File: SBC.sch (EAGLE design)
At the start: 42 parts, among them IC1 MAX3232CPE, IC2 74LS04N, IC3 74LS00N, IC5 NE555P, J1 POWER_JACKPTH, J2 COMPUTER-PERIPHERAL-POWERRA, J3 22-27-2021-02

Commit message: Added gerber files
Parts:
- C7: value (none) -> 10uF
- RAM: value (none) -> 62256
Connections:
- removed net N$32: IC1G$1.T1IN
- removed net N$33: ACIAG$1.RXC, IC1G$1.T1OUT
- removed net RINGINDICATOR: X1.9
- removed net TRANSMITDATA: IC1G$1.R2OUT, X1.3
- new net DATASETREADY: ACIAG$1./DSR, X1.6
- new net N$1: LED1.C, R5.1
- new net N$3: IC1G$1.T1OUT, X1.3
- new net N$5: ACIAG$1.R/W, CPUG$1.R/W
- new net N$7: ACIAG$1.TXD, IC1G$1.T1IN
- new net N$8: ACIAG$1.RXD, IC1G$1.R1OUT
- net DATACARRIERDETECT: now also ACIAG$1./DCD; no longer X1.6
- net DTEREADY: no longer IC1G$1.R2IN
- net GND: now also RAM.VSS, X1.9; no longer ACIAG$1./DCD, ACIAG$1./DSR
- net IRQ: now also ACIAG$1./IRQ, VIA0G$1./IRQ
- net N$17: now also VIA0G$1./CS2
- net RECEIVEDATA: now also IC1G$1.R1IN
- net VCC: now also RAM.VCC; no longer LED1.C, R5.1
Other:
- moved on the sheet: ACIA, C1, C2, C3, C4, C5, C6, C7, C8, C9, CPU, D1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

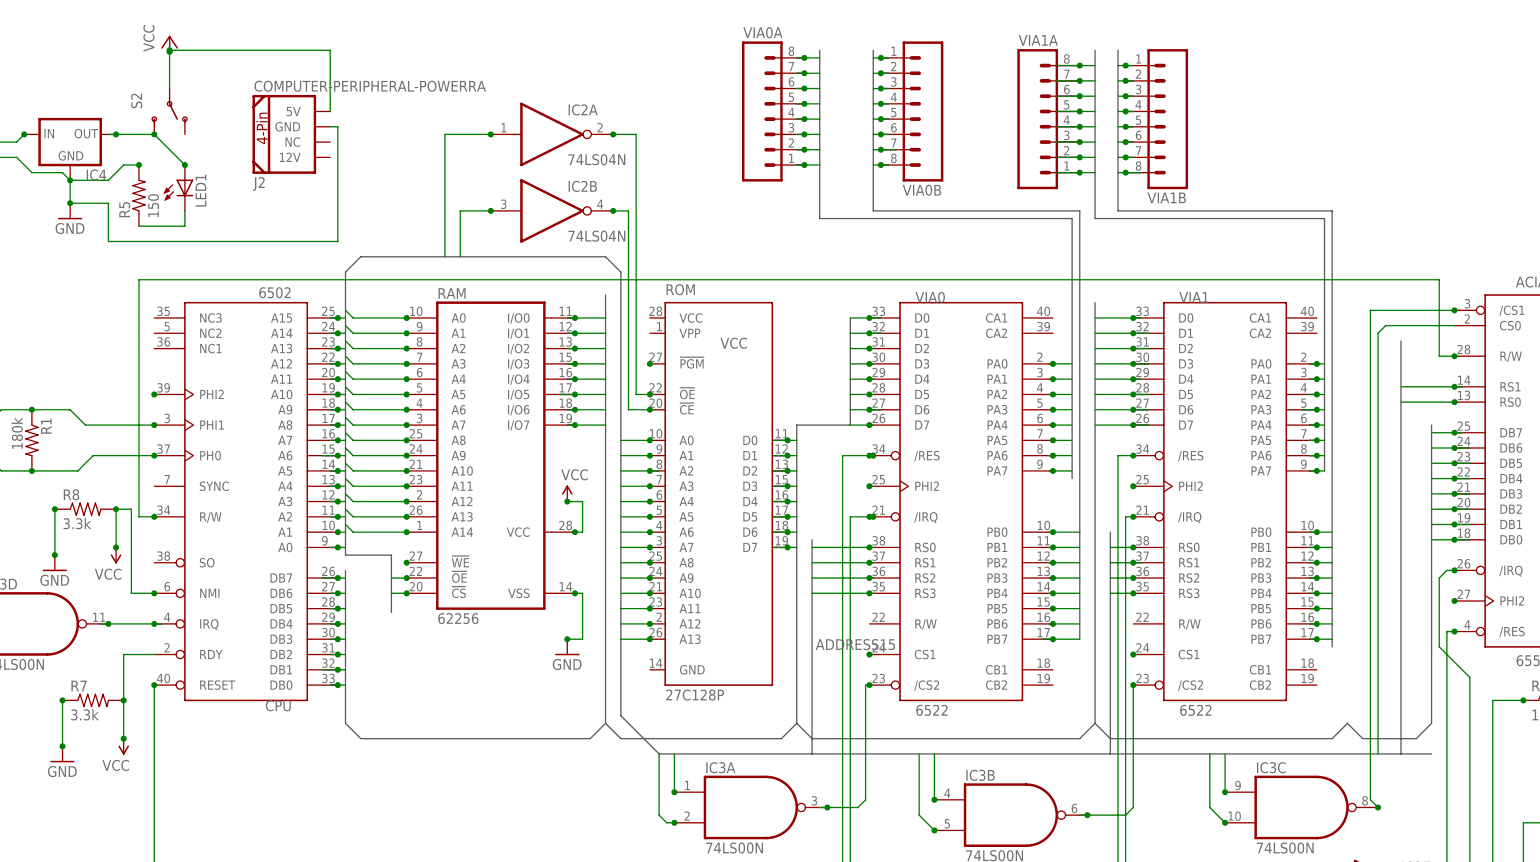
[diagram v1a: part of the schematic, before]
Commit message: Fixed issue with SMD switch
Updated schematic, board, BOM & gerbers for through-hole switch. Sent
gerber off to production.
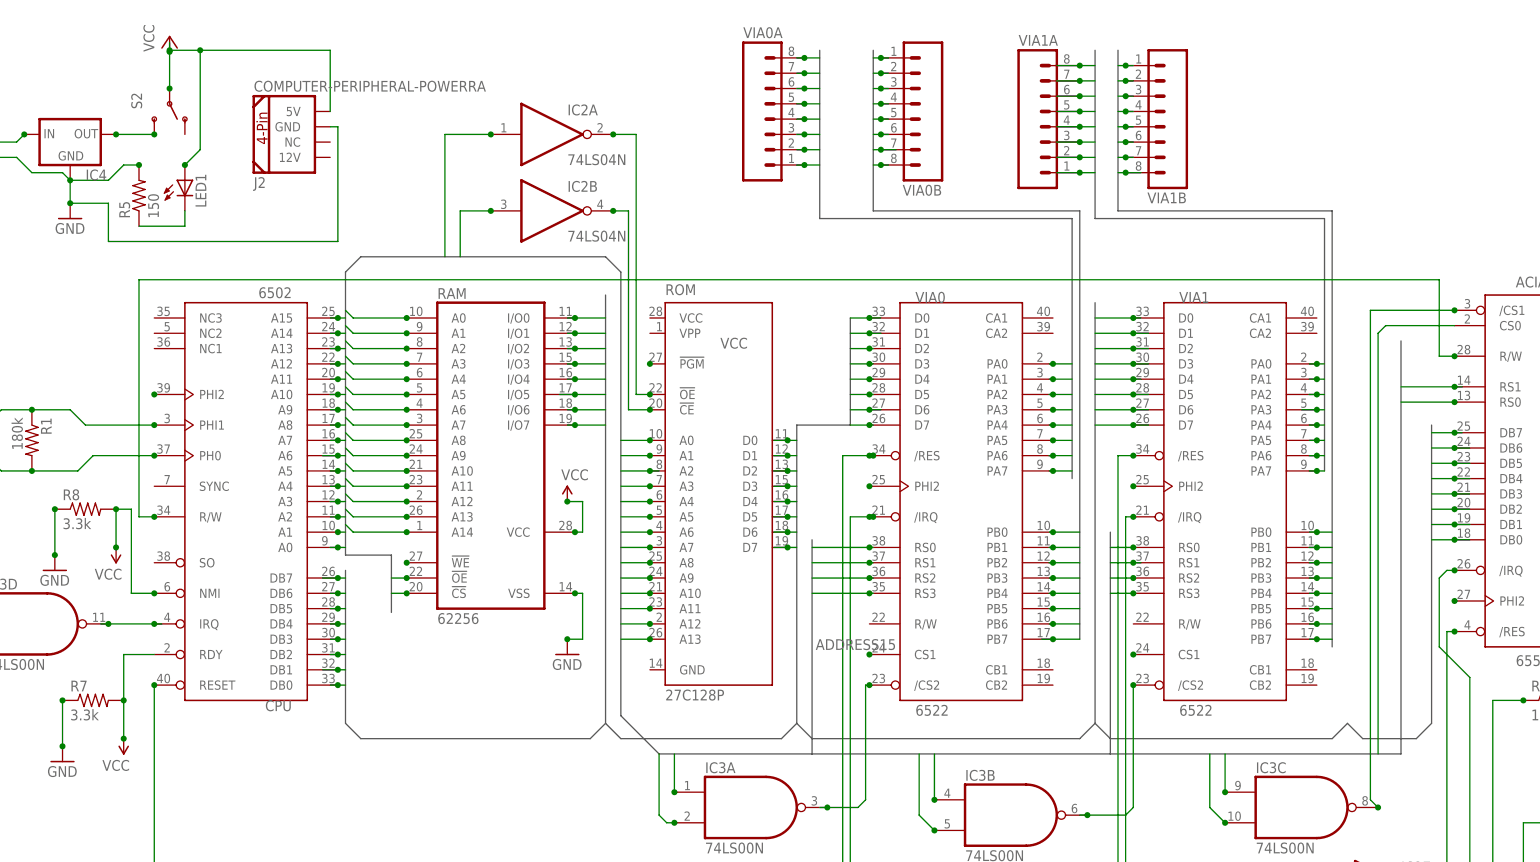
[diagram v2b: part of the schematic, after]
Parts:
- S2: device SparkFun-Electromechanical:SWITCH-SPDTSMD2 -> SparkFun-Electromechanical:SWITCH-SPDTPTH_LOCK
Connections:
- removed net N$28: IC4.OUT, LED1.A, S2.S
- new net N$32: IC4.OUT, S2.S
- net VCC: now also LED1.A
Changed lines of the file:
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@@
 <part name="R4" library="SparkFun-Resistors" deviceset="RESISTOR" device="AXIAL-0.3" value="47k"/>
 <part name="D1" library="SparkFun-DiscreteSemi" deviceset="DIODE" device="1N4148"/>
-<part name="S2" library="SparkFun-Electromechanical" deviceset="SWITCH-SPDT" device="SMD2"/>
 <part name="LED1" library="led" deviceset="LED" device="3MM"/>
 <part name="R5" library="SparkFun-Passives" deviceset="RESISTOR" device="EZ" value="150"/>
@@
 <part name="GND7" library="SparkFun-Aesthetics" deviceset="GND" device=""/>
 <part name="GND8" library="SparkFun-Aesthetics" deviceset="GND" device=""/>
+<part name="S2" library="SparkFun-Electromechanical" deviceset="SWITCH-SPDT" device="PTH_LOCK"/>
 </parts>
 <sheets>
@@
 <instance part="R4" gate="G$1" x="323.85" y="57.15"/>
 <instance part="D1" gate="G$1" x="331.47" y="54.61"/>
-<instance part="S2" gate="1" x="78.74" y="158.75" rot="R270"/>
 <instance part="LED1" gate="G$1" x="81.28" y="146.05"/>
 <instance part="R5" gate="G$1" x="73.66" y="143.51" rot="R90"/>
@@
 <instance part="GND7" gate="1" x="144.78" y="67.31"/>
 <instance part="GND8" gate="1" x="359.41" y="58.42"/>
+<instance part="S2" gate="1" x="78.74" y="158.75" rot="R270"/>
 </instances>
 <busses>
@@
 <wire x1="185.42" y1="50.8" x2="234.95" y2="50.8" width="0.762" layer="92"/>
 <wire x1="234.95" y1="50.8" x2="283.21" y2="50.8" width="0.762" layer="92"/>
-<wire x1="283.21" y1="50.8" x2="288.29" y2="50.8" width="0.762" layer="92"/>
 <wire x1="107.95" y1="83.82" x2="115.57" y2="83.82" width="0.762" layer="92"/>
 <wire x1="115.57" y1="83.82" x2="115.57" y2="74.295" width="0.762" layer="92"/>
@@
 </segment>
 <segment>
-<pinref part="S2" gate="1" pin="P"/>
 <wire x1="78.74" y1="168.91" x2="78.74" y2="167.64" width="0.1524" layer="91"/>
 <pinref part="P+1" gate="VCC" pin="VCC"/>
@@
 <wire x1="78.74" y1="167.64" x2="78.74" y2="167.386" width="0.1524" layer="91"/>
 <wire x1="78.74" y1="167.386" x2="78.74" y2="161.29" width="0.1524" layer="91"/>
+<pinref part="S2" gate="1" pin="P"/>
 <pinref part="J2" gate="G$1" pin="5V"/>
 <wire x1="105.41" y1="157.48" x2="105.41" y2="167.64" width="0.1524" layer="91"/>
-<wire x1="105.41" y1="167.64" x2="78.74" y2="167.64" width="0.1524" layer="91"/>
+<wire x1="78.74" y1="167.64" x2="83.82" y2="167.64" width="0.1524" layer="91"/>
 <junction x="78.74" y="167.64"/>
+<pinref part="LED1" gate="G$1" pin="A"/>
+<wire x1="83.82" y1="167.64" x2="105.41" y2="167.64" width="0.1524" layer="91"/>
+<wire x1="81.28" y1="148.59" x2="81.28" y2="148.336" width="0.1524" layer="91"/>
+<wire x1="81.28" y1="148.59" x2="83.82" y2="151.13" width="0.1524" layer="91"/>
+<junction x="81.28" y="148.59"/>
+<wire x1="83.82" y1="151.13" x2="83.82" y2="167.64" width="0.1524" layer="91"/>
+<junction x="83.82" y="167.64"/>
+<junction x="78.74" y="161.29"/>
 </segment>
 <segment>
@@
 </segment>
 </net>
-<net name="N$28" class="0">
-<segment>
-<pinref part="S2" gate="1" pin="S"/>
-<wire x1="68.58" y1="153.67" x2="69.85" y2="153.67" width="0.1524" layer="91"/>
-<junction x="76.2" y="153.67"/>
-<pinref part="IC4" gate="G$1" pin="OUT"/>
-<junction x="69.85" y="153.67"/>
-<wire x1="69.85" y1="153.67" x2="76.2" y2="153.67" width="0.1524" layer="91"/>
-<pinref part="LED1" gate="G$1" pin="A"/>
-<wire x1="76.2" y1="153.67" x2="81.28" y2="148.59" width="0.1524" layer="91"/>
-<junction x="81.28" y="148.59"/>
-</segment>
-</net>
 <net name="N$30" class="0">
 <segment>
@@
 </segment>
 </net>
+<net name="N$32" class="0">
+<segment>
+<pinref part="IC4" gate="G$1" pin="OUT"/>
+<pinref part="S2" gate="1" pin="S"/>
+<wire x1="69.85" y1="153.67" x2="76.2" y2="153.67" width="0.1524" layer="91"/>
+<junction x="69.85" y="153.67"/>
+<junction x="76.2" y="153.67"/>
+</segment>
+</net>
